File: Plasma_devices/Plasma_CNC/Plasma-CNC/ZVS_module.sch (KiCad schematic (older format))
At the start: 0 parts

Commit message: Updaged electrical
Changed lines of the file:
@@
 $Descr A4 11693 8268
 encoding utf-8
-Sheet 4 8
+Sheet 3 8
 Title ""
 Date ""
@@
 $EndDescr
 Text HLabel 1450 1100 0    50   Input ~ 0
-LINE
++LVin
 Text HLabel 1450 1250 0    50   Input ~ 0
-NEUTRAL
-Text HLabel 1450 1400 0    50   Input ~ 0
-PE
-Text HLabel 1450 1800 0    50   Output ~ 0
-HVon
-Text HLabel 1450 1900 0    50   Output ~ 0
-AIRon
-Text HLabel 1450 1600 0    50   Input ~ 0
-USBin
-Text HLabel 1450 2000 0    50   Output ~ 0
-SIG-GND
+-LVin
+Text HLabel 2050 1100 2    50   Output ~ 0
+HVACout1
+Text HLabel 2050 1250 2    50   Output ~ 0
+HVACout2
 $EndSCHEMATC

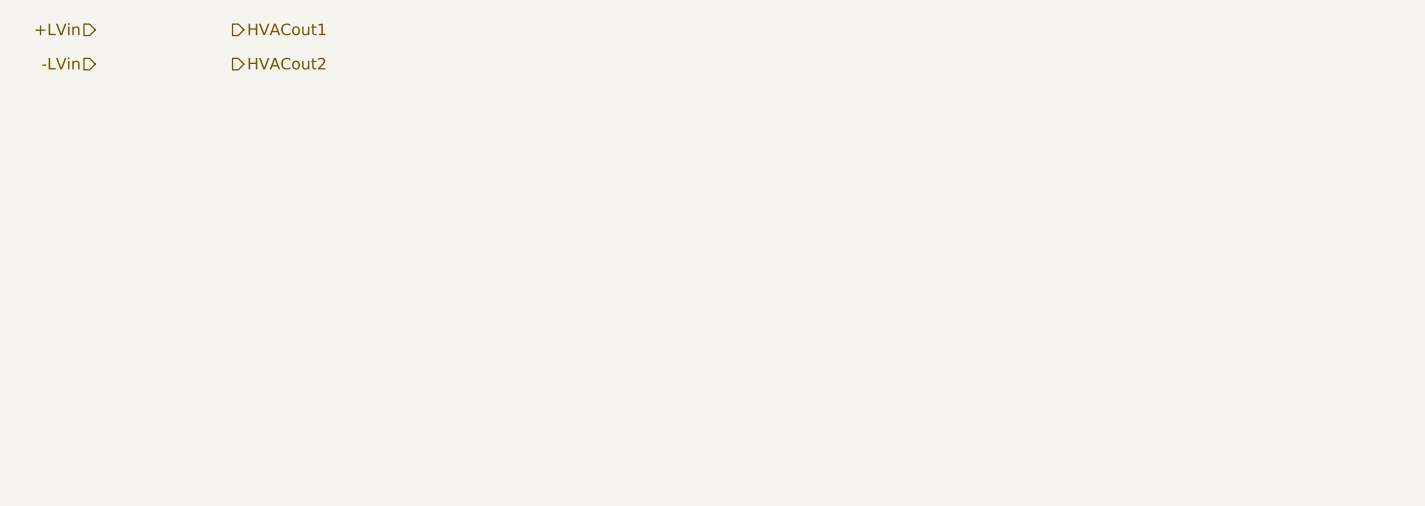
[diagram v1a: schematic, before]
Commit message: ZVS circuit included
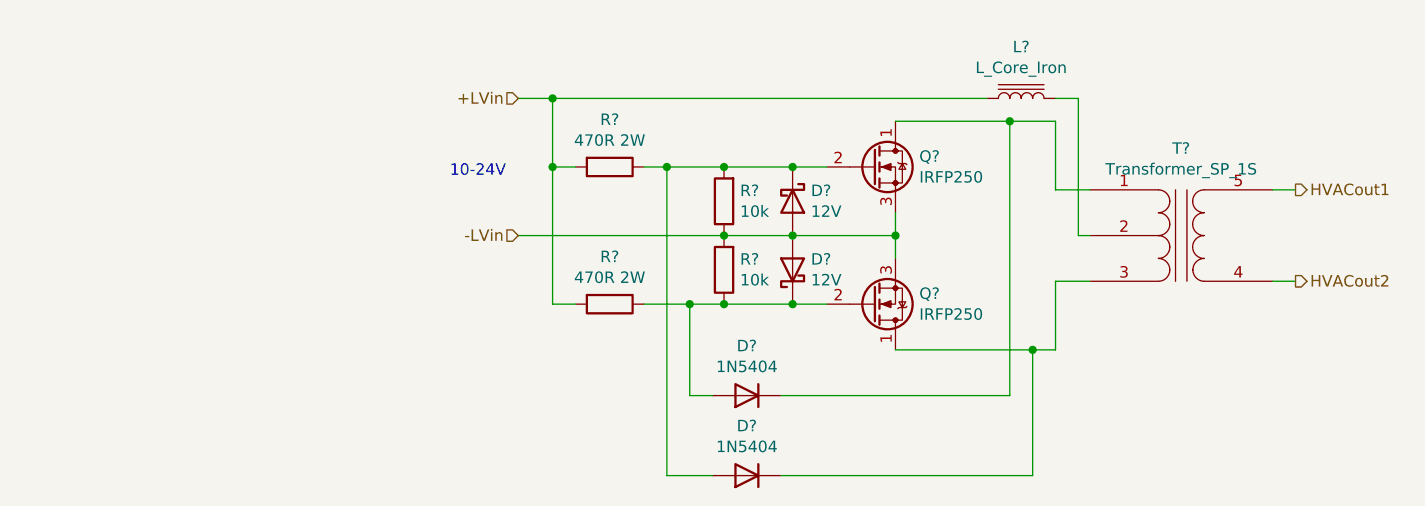
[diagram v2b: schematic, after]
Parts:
- added D? (x2): 1N5404, symbol Device:D
- added D? (x2): 12V, symbol Device:D_Schottky
- added L?: L_Core_Iron, symbol Device:L_Core_Iron
- added Q? (x2): IRFP250, Package_DirectFET:DirectFET_MF, symbol Transistor_FET:IRF40DM229
- added R? (x2): 470R 2W, symbol Device:R
- added R? (x2): 10k, symbol Device:R
- added T?: Transformer_SP_1S, symbol Device:Transformer_SP_1S
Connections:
- net +LVin: now also L?.1, R?.2, R?.2
- net -LVin: now also D?.2 (A), D?.2 (A), Q?.3 (S), Q?.3 (S), R?.1, R?.2
- net HVACout1: now also T?.5 (S2)
- net HVACout2: now also T?.4 (S1)
- new net: D?.1 (K), Q?.1 (D), T?.1 (PR1)
- new net: D?.1 (K), D?.2 (A), Q?.2 (G), R?.1, R?.2
- new net: D?.1 (K), Q?.1 (D), T?.3 (PR2)
- new net: D?.1 (K), D?.2 (A), Q?.2 (G), R?.1, R?.1
- new net: L?.2, T?.2 (PM)
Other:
- note added: "10-24V"
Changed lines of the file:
@@
 Comment4 ""
 $EndDescr
-Text HLabel 1450 1100 0    50   Input ~ 0
+Text HLabel 3300 1400 0    50   Input ~ 0
 +LVin
-Text HLabel 1450 1250 0    50   Input ~ 0
+Text HLabel 3300 2000 0    50   Input ~ 0
 -LVin
-Text HLabel 2050 1100 2    50   Output ~ 0
+Text HLabel 6700 1800 2    50   Output ~ 0
 HVACout1
-Text HLabel 2050 1250 2    50   Output ~ 0
+Text HLabel 6700 2200 2    50   Output ~ 0
 HVACout2
+Text Notes 3000 1750 0    50   ~ 0
+10-24V
+$Comp
+L Transistor_FET:IRF40DM229 Q?
+U 1 1 5F686801
+P 4850 1700
+F 0 "Q?" H 5054 1746 50  0000 L CNN
+F 1 "IRFP250" H 5054 1655 50  0000 L CNN
+F 2 "Package_DirectFET:DirectFET_MF" H 4850 1700 50  0001 C CIN
+F 3 "https://www.infineon.com/dgdl/Infineon-IRF40DM229-DS-v02_00-EN.pdf?fileId=5546d462557e6e890155a15c899160ea" H 4850 1700 50  0001 L CNN
+	1    4850 1700
+	1    0    0    -1
+$EndComp
+$Comp
+L Transistor_FET:IRF40DM229 Q?
+U 1 1 5F687145
+P 4850 2300
+F 0 "Q?" H 5054 2254 50  0000 L CNN
+F 1 "IRFP250" H 5054 2345 50  0000 L CNN
+F 2 "Package_DirectFET:DirectFET_MF" H 4850 2300 50  0001 C CIN
+F 3 "https://www.infineon.com/dgdl/Infineon-IRF40DM229-DS-v02_00-EN.pdf?fileId=5546d462557e6e890155a15c899160ea" H 4850 2300 50  0001 L CNN
+	1    4850 2300
+	1    0    0    1
+$EndComp
+$Comp
+L Device:R R?
+U 1 1 5F6876B6
+P 3700 1700
+F 0 "R?" V 3493 1700 50  0000 C CNN
+F 1 "470R 2W" V 3584 1700 50  0000 C CNN
+F 2 "" V 3630 1700 50  0001 C CNN
+F 3 "~" H 3700 1700 50  0001 C CNN
+	1    3700 1700
+	0    1    1    0
+$EndComp
+$Comp
+L Device:R R?
+U 1 1 5F687A03
+P 3700 2300
+F 0 "R?" V 3493 2300 50  0000 C CNN
+F 1 "470R 2W" V 3584 2300 50  0000 C CNN
+F 2 "" V 3630 2300 50  0001 C CNN
+F 3 "~" H 3700 2300 50  0001 C CNN
+	1    3700 2300
+	0    1    1    0
+$EndComp
+$Comp
+L Device:R R?
+U 1 1 5F687CEB
+P 4200 1850
+F 0 "R?" H 4130 1804 50  0000 R CNN
+F 1 "10k" H 4130 1895 50  0000 R CNN
+F 2 "" V 4130 1850 50  0001 C CNN
+F 3 "~" H 4200 1850 50  0001 C CNN
+	1    4200 1850
+	-1   0    0    1
+$EndComp
+$Comp
+L Device:R R?
+U 1 1 5F687FF5
+P 4200 2150
+F 0 "R?" H 4130 2104 50  0000 R CNN
+F 1 "10k" H 4130 2195 50  0000 R CNN
+F 2 "" V 4130 2150 50  0001 C CNN
+F 3 "~" H 4200 2150 50  0001 C CNN
+	1    4200 2150
+	-1   0    0    1
+$EndComp
+$Comp
+L Device:D D?
+U 1 1 5F688538
+P 4300 2700
+F 0 "D?" H 4300 2483 50  0000 C CNN
+F 1 "1N5404" H 4300 2574 50  0000 C CNN
+F 2 "" H 4300 2700 50  0001 C CNN
+F 3 "~" H 4300 2700 50  0001 C CNN
+	1    4300 2700
+	-1   0    0    1
+$EndComp
+Wire Wire Line
+	4200 1700 4500 1700
+Connection ~ 4500 1700
+Wire Wire Line
+	4500 1700 4650 1700
+Wire Wire Line
+	4650 2300 4500 2300
+Connection ~ 4500 2300
+Wire Wire Line
+	4500 2300 4200 2300
+Wire Wire Line
+	4950 2000 4950 2100
+Connection ~ 4200 2000
+Connection ~ 4500 2000
+Wire Wire Line
+	4500 2000 4950 2000
+Wire Wire Line
+	4950 1900 4950 2000
+Connection ~ 4950 2000
+Wire Wire Line
+	3550 2300 3450 2300
+Wire Wire Line
+	3450 1700 3550 1700
+$Comp
+L Device:Transformer_SP_1S T?
+U 1 1 5F68CD2A
+P 6200 2000
+F 0 "T?" H 6200 2381 50  0000 C CNN
+F 1 "Transformer_SP_1S" H 6200 2290 50  0000 C CNN
+F 2 "" H 6200 2000 50  0001 C CNN
+F 3 "~" H 6200 2000 50  0001 C CNN
+	1    6200 2000
+	1    0    0    -1
+$EndComp
+Wire Wire Line
+	5800 2000 5750 2000
+Wire Wire Line
+	5800 2200 5650 2200
+Wire Wire Line
+	5650 2200 5650 2500
+Wire Wire Line
+	5800 1800 5650 1800
+Wire Wire Line
+	5650 1800 5650 1500
+Wire Wire Line
+	4950 1500 5450 1500
+Wire Wire Line
+	4950 2500 5550 2500
+$Comp
+L Device:L_Core_Iron L?
+U 1 1 5F692959
+P 5500 1400
+F 0 "L?" V 5725 1400 50  0000 C CNN
+F 1 "L_Core_Iron" V 5634 1400 50  0000 C CNN
+F 2 "" H 5500 1400 50  0001 C CNN
+F 3 "~" H 5500 1400 50  0001 C CNN
+	1    5500 1400
+	0    -1   -1   0
+$EndComp
+Wire Wire Line
+	5750 1400 5650 1400
+Wire Wire Line
+	3300 1400 3450 1400
+Connection ~ 3450 1700
+Connection ~ 3450 1400
+Wire Wire Line
+	3850 2300 4050 2300
+Connection ~ 4200 2300
+Wire Wire Line
+	4200 2000 4500 2000
+Wire Wire Line
+	3300 2000 4200 2000
+Wire Wire Line
+	3850 1700 3950 1700
+Connection ~ 4200 1700
+Wire Wire Line
+	6700 2200 6600 2200
+Wire Wire Line
+	6600 1800 6700 1800
+Wire Wire Line
+	3450 1400 5350 1400
+Wire Wire Line
+	5750 1400 5750 2000
+Wire Wire Line
+	3450 1700 3450 1400
+$Comp
+L Device:D_Schottky D?
+U 1 1 5F69C375
+P 4500 1850
+F 0 "D?" V 4454 1930 50  0000 L CNN
+F 1 "12V" V 4545 1930 50  0000 L CNN
+F 2 "" H 4500 1850 50  0001 C CNN
+F 3 "~" H 4500 1850 50  0001 C CNN
+	1    4500 1850
+	0    1    1    0
+$EndComp
+$Comp
+L Device:D_Schottky D?
+U 1 1 5F69C861
+P 4500 2150
+F 0 "D?" V 4546 2070 50  0000 R CNN
+F 1 "12V" V 4455 2070 50  0000 R CNN
+F 2 "" H 4500 2150 50  0001 C CNN
+F 3 "~" H 4500 2150 50  0001 C CNN
+	1    4500 2150
+	0    -1   -1   0
+$EndComp
+$Comp
+L Device:D D?
+U 1 1 5F69DC1B
+P 4300 3050
+F 0 "D?" H 4300 2833 50  0000 C CNN
+F 1 "1N5404" H 4300 2924 50  0000 C CNN
+F 2 "" H 4300 3050 50  0001 C CNN
+F 3 "~" H 4300 3050 50  0001 C CNN
+	1    4300 3050
+	-1   0    0    1
+$EndComp
+Wire Wire Line
+	3950 1700 3950 3050
+Wire Wire Line
+	3950 3050 4150 3050
+Wire Wire Line
+	3450 1700 3450 2300
+Connection ~ 3950 1700
+Wire Wire Line
+	3950 1700 4200 1700
+Wire Wire Line
+	4150 2700 4050 2700
+Wire Wire Line
+	4050 2700 4050 2300
+Connection ~ 4050 2300
+Wire Wire Line
+	4050 2300 4200 2300
+Wire Wire Line
+	4450 2700 5450 2700
+Wire Wire Line
+	5450 2700 5450 1500
+Connection ~ 5450 1500
+Wire Wire Line
+	5450 1500 5650 1500
+Wire Wire Line
+	4450 3050 5550 3050
+Wire Wire Line
+	5550 3050 5550 2500
+Connection ~ 5550 2500
+Wire Wire Line
+	5550 2500 5650 2500
 $EndSCHEMATC

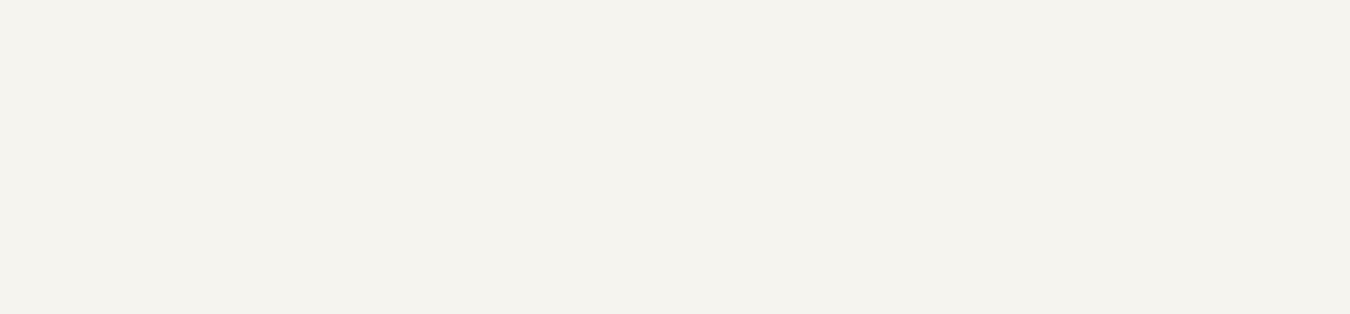
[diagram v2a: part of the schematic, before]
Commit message: DVS module included
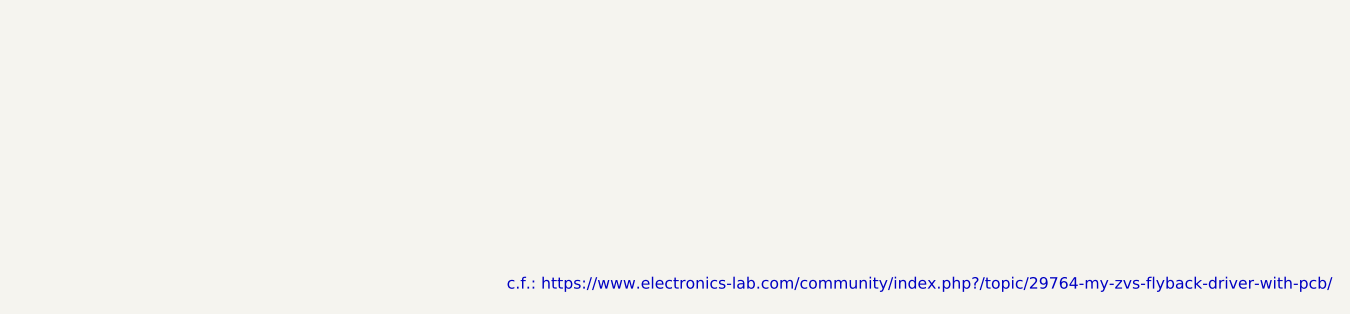
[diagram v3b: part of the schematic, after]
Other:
- note added: "c.f.: https://www.electronics-lab.com/community/index.php?/topic/29764-my-zvs-flyback-driver-with-pcb/"
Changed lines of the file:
@@
 Wire Wire Line
 	5550 2500 5650 2500
+Text Notes 10950 6250 2    50   ~ 0
+c.f.: https://www.electronics-lab.com/community/index.php?/topic/29764-my-zvs-flyback-driver-with-pcb/
 $EndSCHEMATC
